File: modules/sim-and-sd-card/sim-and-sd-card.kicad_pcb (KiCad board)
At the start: 2 copper layers, 22.8 x 27 mm, 2 parts

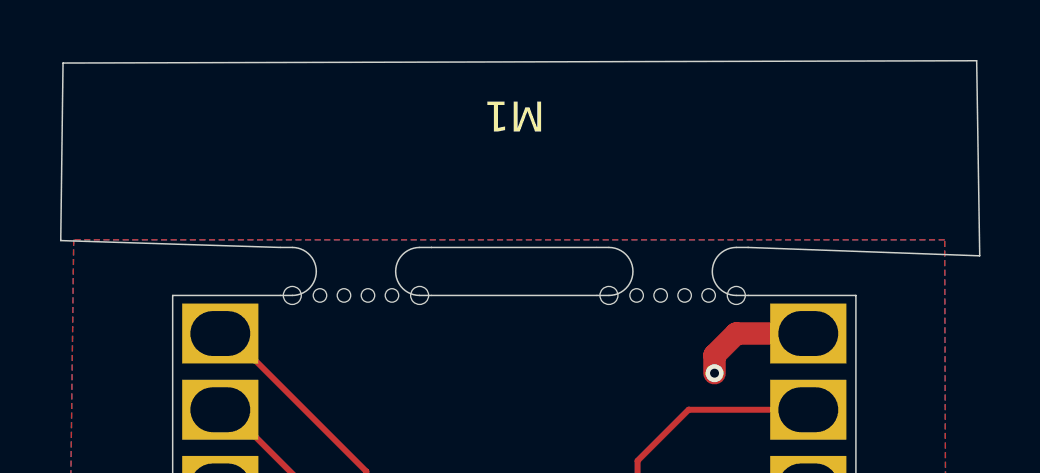
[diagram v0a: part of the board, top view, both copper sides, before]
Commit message: exported gerbers for SIM SD card module
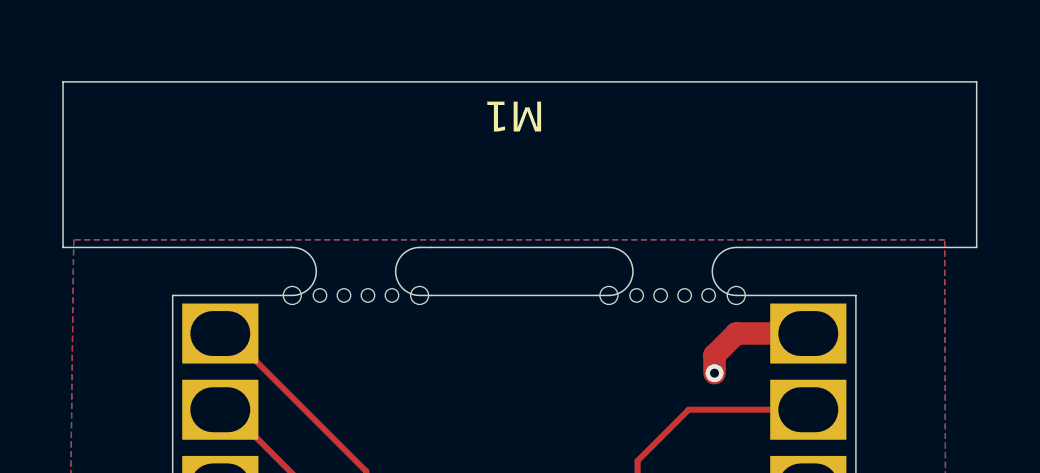
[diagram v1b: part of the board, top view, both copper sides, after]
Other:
- board text added: "Molex 104168-1616"
- board text added: "github.com/gardners/ megaphone-r5-modular R20250225"
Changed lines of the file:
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@@
 			(outputformat 1)
 			(mirror no)
-			(drillshape 1)
+			(drillshape 0)
 			(scaleselection 1)
-			(outputdirectory "")
+			(outputdirectory "gerbers/")
 		)
 	)
@@
 	)
 	(gr_line
-		(start 44.6024 34.29)
-		(end 44.6786 28.3718)
+		(start 44.6786 29)
+		(end 44.6786 34.5188)
 		(stroke
 			(width 0.05)
@@
 	)
 	(gr_line
-		(start 44.6786 28.3718)
-		(end 75.1332 28.2956)
+		(start 44.6786 29)
+		(end 75.1332 29)
 		(stroke
 			(width 0.05)
@@
 	(gr_line
 		(start 51.9208 34.5188)
-		(end 44.6024 34.29)
+		(end 44.6786 34.5188)
 		(stroke
 			(width 0.05)
@@
 	)
 	(gr_line
-		(start 75.1332 28.2956)
-		(end 75.2348 34.798)
+		(start 75.1332 29)
+		(end 75.1332 34.5188)
 		(stroke
 			(width 0.05)
@@
 	)
 	(gr_line
-		(start 75.2348 34.798)
+		(start 75.1332 34.5188)
 		(end 67.511 34.5188)
 		(stroke
@@
 		(layer "Edge.Cuts")
 	)
+	(gr_text "Molex 104168-1616"
+		(at 62.7634 40.767 90)
+		(layer "B.SilkS")
+		(effects
+			(font
+				(size 1 1)
+				(thickness 0.1)
+			)
+			(justify left bottom mirror)
+		)
+	)
+	(gr_text "github.com/gardners/\nmegaphone-r5-modular\nR20250225"
+		(at 59.7208 38.5188 90)
+		(layer "B.SilkS")
+		(effects
+			(font
+				(size 1 1)
+				(thickness 0.1)
+			)
+			(justify left bottom mirror)
+		)
+	)
 	(segment

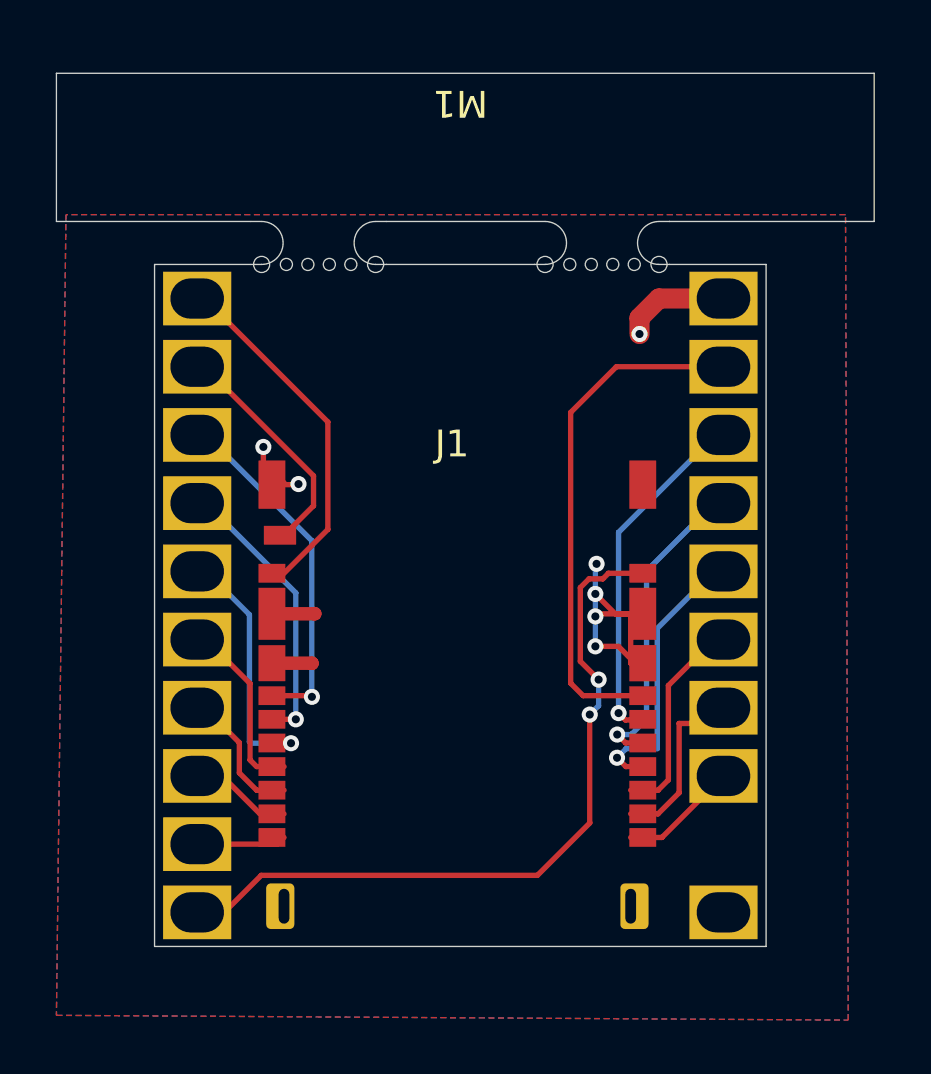
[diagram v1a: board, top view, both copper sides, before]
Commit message: KiCad v9 adding new footprints
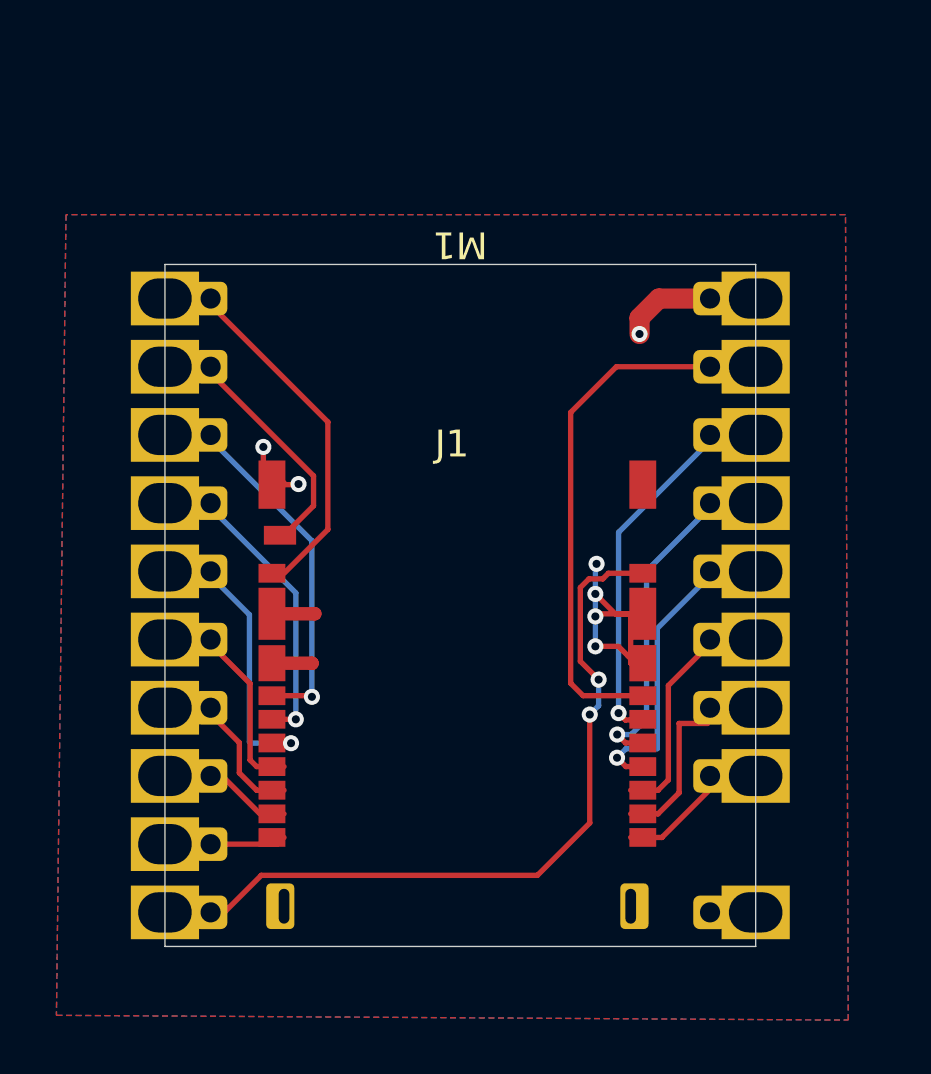
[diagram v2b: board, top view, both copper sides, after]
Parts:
- M1: footprint MegaCastle:MegaCastle2x10-Module-I16.0x20.6-MBFFFF-PANEL-NIBBLE -> MegaCastle:MegaCastle2x10-Module-I22.0x20.6-MBFFFF-SPAREPAD
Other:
- board size 22.8 x 27 mm -> 22 x 25.4 mm
